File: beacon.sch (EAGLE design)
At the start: 49 parts, among them J1 5-5530843-0MALE, Q1 MMBT3904, Q2 DMG2302UK, U1 AOZ6662DI, U3 ATTINY85, U4 MS5637-02BA03, U5 SI4012, U6 MAAL-010704, U7 MIC5504

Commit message: Initial version of tracker schematic
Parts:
- R13: value 0R -> TBD
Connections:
- removed net DETECT: J1.5
- net OC1B: now also J1.5
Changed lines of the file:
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@@
 <part name="P+13" library="radio-tracker" deviceset="+3V3" device=""/>
 <part name="D1" library="radio-tracker" deviceset="LED" device=""/>
-<part name="R13" library="radio-tracker" deviceset="RESISTOR" device="0603" value="0R"/>
+<part name="R13" library="radio-tracker" deviceset="RESISTOR" device="0603" value="TBD"/>
 <part name="P+14" library="radio-tracker" deviceset="+3V3" device=""/>
 <part name="Z1" library="radio-tracker" deviceset="ABT-8" device="" package3d_urn="urn:adsk.eagle:package:18040019/1"/>
@@
 <label x="15.24" y="0" size="1.778" layer="95"/>
 </segment>
+<segment>
+<pinref part="J1" gate="G$1" pin="5"/>
+<wire x1="66.04" y1="5.08" x2="48.26" y2="5.08" width="0.1524" layer="91"/>
+<label x="48.26" y="5.08" size="1.778" layer="95"/>
+</segment>
 </net>
 <net name="VBAT" class="0">
@@
 </segment>
 </net>
-<net name="DETECT" class="0">
-<segment>
-<pinref part="J1" gate="G$1" pin="5"/>
-<wire x1="66.04" y1="5.08" x2="48.26" y2="5.08" width="0.1524" layer="91"/>
-<label x="48.26" y="5.08" size="1.778" layer="95"/>
-</segment>
-</net>

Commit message: Various schematic updates
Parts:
- LS1: value WT-1205 -> AT-1224-TWT-5V-2-R; device radio-tracker:WT-1205 -> radio-tracker:AT-1224-TWT-5V-2-R
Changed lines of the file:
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@@
 <part name="R12" library="radio-tracker" deviceset="RESISTOR" device="0603" value="1M"/>
 <part name="C14" library="radio-tracker" deviceset="CAPACITOR" device="0603" value="0.1uF"/>
-<part name="LS1" library="radio-tracker" deviceset="WT-1205" device="" package3d_urn="urn:adsk.eagle:package:18040044/1"/>
+<part name="LS1" library="radio-tracker" deviceset="AT-1224-TWT-5V-2-R" device="" package3d_urn="urn:adsk.eagle:package:18040044/1"/>
 <part name="GND20" library="radio-tracker" deviceset="GND" device=""/>
 <part name="P+12" library="radio-tracker" deviceset="+5V" device=""/>

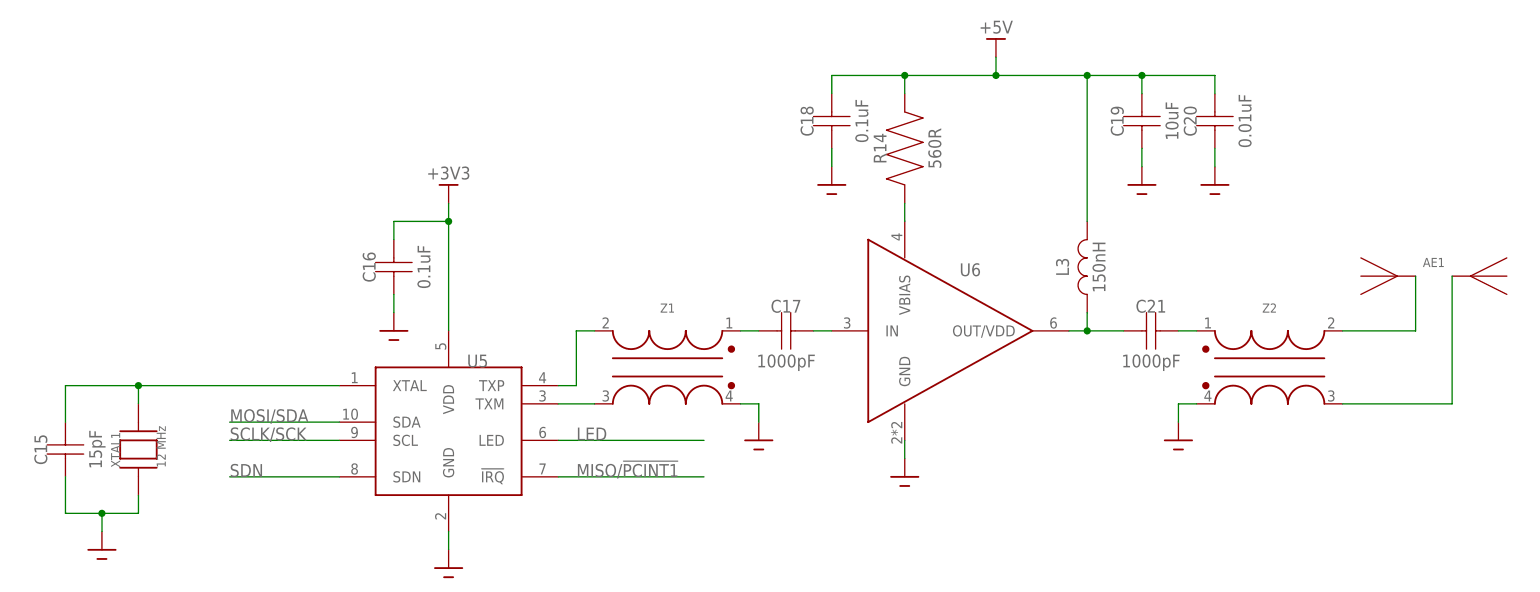
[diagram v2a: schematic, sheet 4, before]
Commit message: First routing attempt
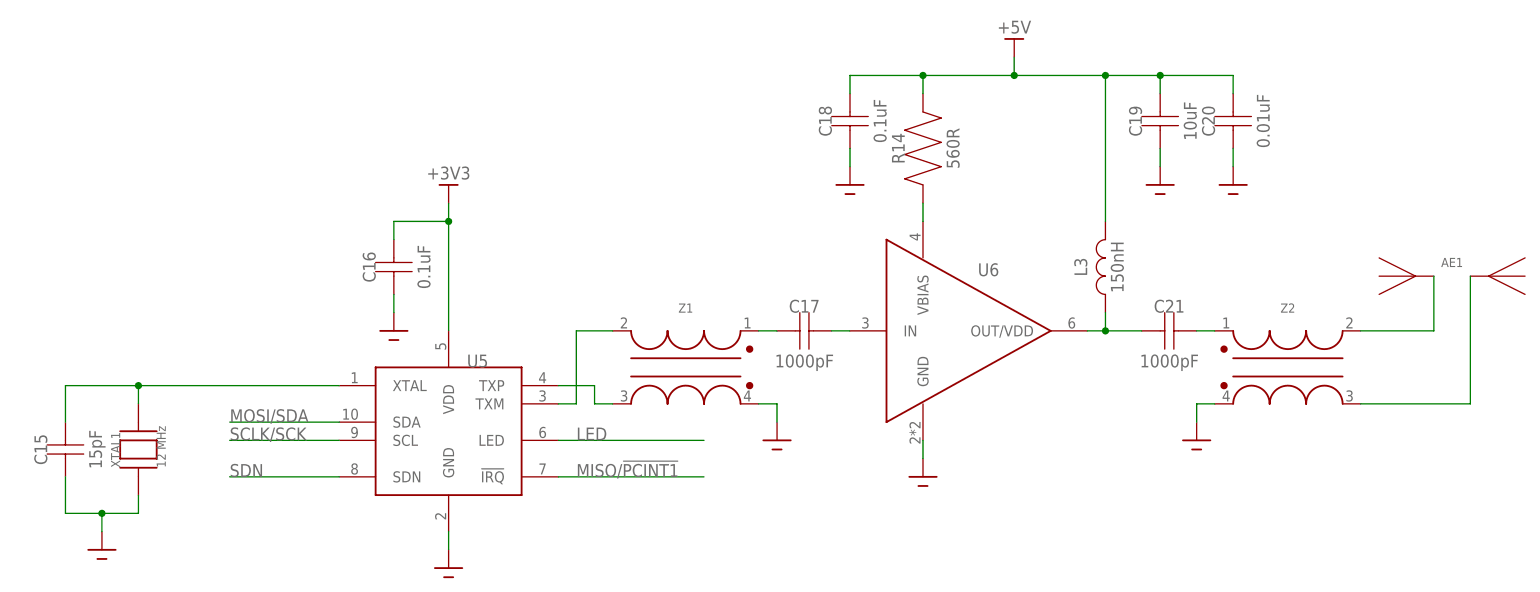
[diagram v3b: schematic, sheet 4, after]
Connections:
- removed net N$18: U5.TXM, Z1.BAL2
- removed net N$19: U5.TXP, Z1.BAL1
- new net N$10: U5.TXP, Z1.BAL2
- new net N$11: U5.TXM, Z1.BAL1
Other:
- moved on the sheet: AE1, C17, C18, C19, C20, C21, L3, R14, U6, Z1, Z2

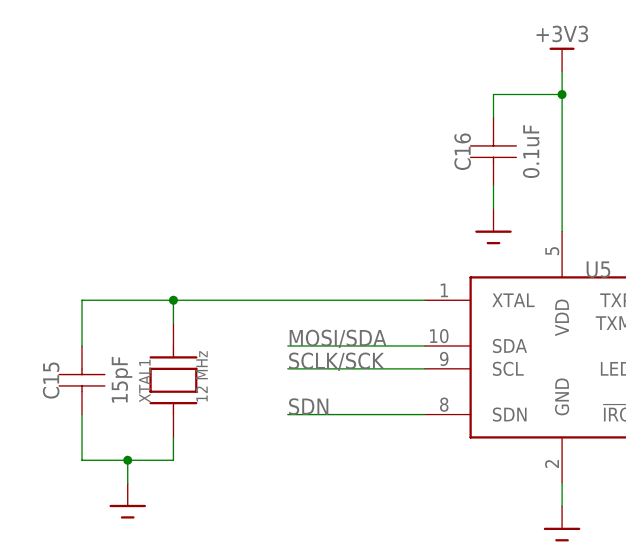
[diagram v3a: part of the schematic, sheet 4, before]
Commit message: Routed beacon
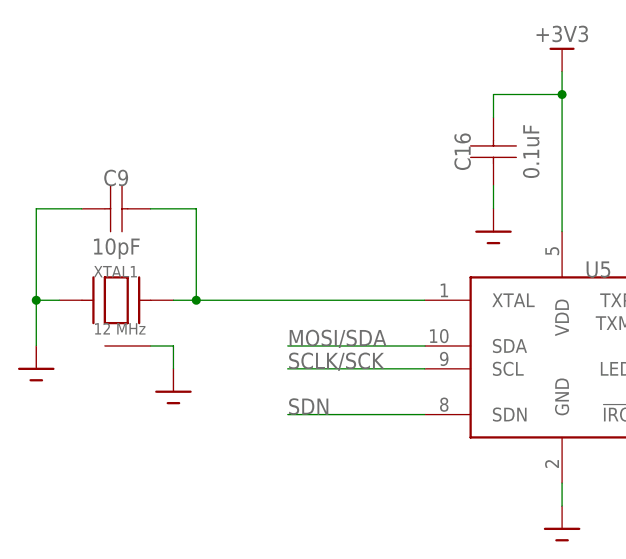
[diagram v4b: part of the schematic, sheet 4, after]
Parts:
- removed C15: 15pF, radio-tracker:CAPACITOR0603
- added C9: 10pF, radio-tracker:CAPACITOR0603
- XTAL1: device radio-tracker:ABLS -> radio-tracker:RH100
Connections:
- net !RESET: now also J1.9; no longer J1.6
- net +3V3: now also J1.4; no longer J1.1
- net +5V: now also J1.3; no longer J1.2
- net +9V: now also J1.2; no longer J1.3
- net GND: now also C9.P$1, XTAL1.GND; no longer C15.P$1
- net MISO/!PCINT1: now also J1.6; no longer J1.8
- net MOSI/SDA: now also J1.7; no longer J1.9
- net N$17: now also C9.P$2; no longer C15.P$2
- net OC1B: now also J1.8; no longer J1.5
- net SCLK/SCK: now also J1.5; no longer J1.7
- net VBAT: now also J1.1; no longer J1.4

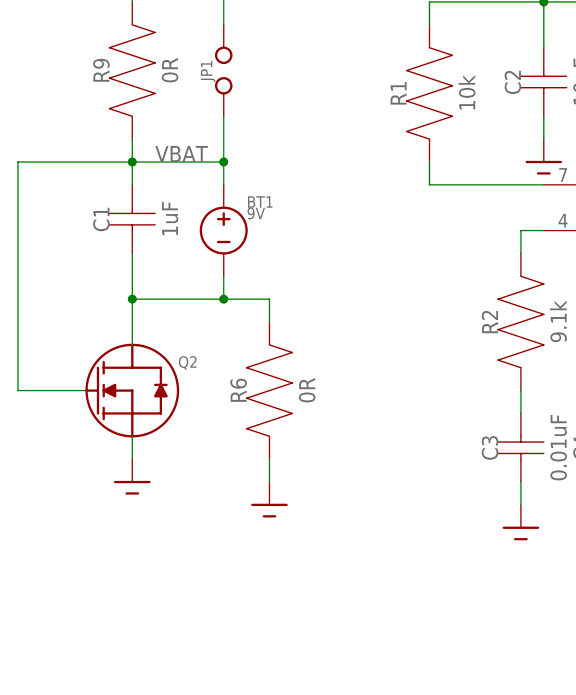
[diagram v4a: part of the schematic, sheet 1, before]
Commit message: Added PTC fuse
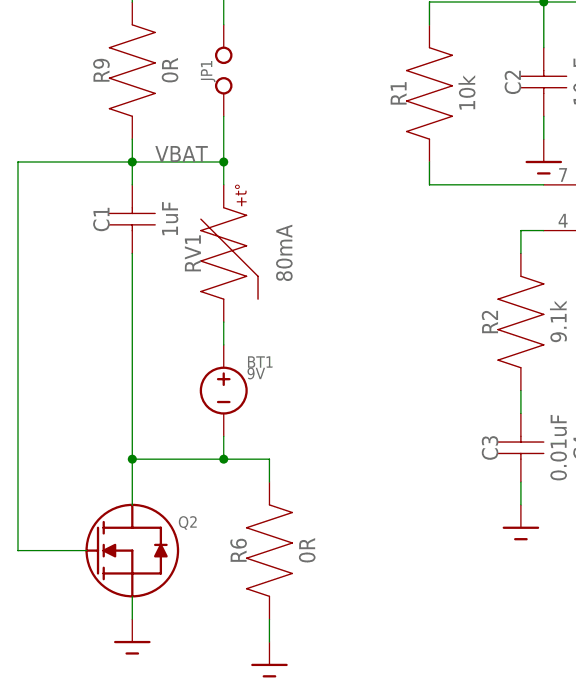
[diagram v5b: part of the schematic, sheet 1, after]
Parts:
- added RV1: 80mA, radio-tracker:PTC0603
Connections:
- new net N$12: BT1.P$2, RV1.P$1
- net VBAT: now also RV1.P$2; no longer BT1.P$2
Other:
- moved on the sheet: BT1, Q2, R6
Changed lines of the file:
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@@
 <part name="C9" library="radio-tracker" deviceset="CAPACITOR" device="0603" value="10pF"/>
 <part name="GND12" library="radio-tracker" deviceset="GND" device=""/>
+<part name="RV1" library="radio-tracker" deviceset="PTC" device="0603" value="80mA"/>
 </parts>
 <sheets>
@@
 </plain>
 <instances>
-<instance part="BT1" gate="G$1" x="2.54" y="-2.54" smashed="yes">
-<attribute name="NAME" x="5.08" y="0" size="1.27" layer="95"/>
-<attribute name="VALUE" x="5.08" y="0" size="1.27" layer="96" align="top-left"/>
-</instance>
-<instance part="GND1" gate="1" x="-7.62" y="-30.48" smashed="yes"/>
+<instance part="BT1" gate="G$1" x="2.54" y="-20.32" smashed="yes">
+<attribute name="NAME" x="5.08" y="-17.78" size="1.27" layer="95"/>
+<attribute name="VALUE" x="5.08" y="-17.78" size="1.27" layer="96" align="top-left"/>
+</instance>
+<instance part="GND1" gate="1" x="-7.62" y="-48.26" smashed="yes"/>
 <instance part="C1" gate="G$1" x="-7.62" y="-5.08" smashed="yes" rot="R90">
 <attribute name="NAME" x="-10.16" y="-1.27" size="1.778" layer="95" rot="R90" align="bottom-center"/>
@@
 <instance part="GND9" gate="1" x="154.94" y="-30.48" smashed="yes"/>
 <instance part="GND10" gate="1" x="175.26" y="-27.94" smashed="yes"/>
-<instance part="Q2" gate="G$1" x="-7.62" y="-20.32" smashed="yes">
-<attribute name="NAME" x="-2.54" y="-17.78" size="1.27" layer="95"/>
-</instance>
-<instance part="R6" gate="G$1" x="7.62" y="-27.94" smashed="yes" rot="R90">
-<attribute name="NAME" x="5.08" y="-20.32" size="1.778" layer="95" rot="R90" align="bottom-center"/>
-<attribute name="VALUE" x="12.7" y="-20.32" size="1.778" layer="96" rot="R90" align="bottom-center"/>
-</instance>
-<instance part="GND11" gate="1" x="7.62" y="-33.02" smashed="yes"/>
+<instance part="Q2" gate="G$1" x="-7.62" y="-38.1" smashed="yes">
+<attribute name="NAME" x="-2.54" y="-35.56" size="1.27" layer="95"/>
+</instance>
+<instance part="R6" gate="G$1" x="7.62" y="-45.72" smashed="yes" rot="R90">
+<attribute name="NAME" x="5.08" y="-38.1" size="1.778" layer="95" rot="R90" align="bottom-center"/>
+<attribute name="VALUE" x="12.7" y="-38.1" size="1.778" layer="96" rot="R90" align="bottom-center"/>
+</instance>
+<instance part="GND11" gate="1" x="7.62" y="-50.8" smashed="yes"/>
+<instance part="RV1" gate="G$1" x="2.54" y="-12.7" smashed="yes" rot="R90">
+<attribute name="NAME" x="0" y="-5.08" size="1.778" layer="95" rot="R90" align="bottom-center"/>
+<attribute name="VALUE" x="10.16" y="-5.08" size="1.778" layer="96" rot="R90" align="bottom-center"/>
+</instance>
 </instances>
 <busses>
@@
 <segment>
 <pinref part="Q2" gate="G$1" pin="S"/>
-<wire x1="-7.62" y1="-25.4" x2="-7.62" y2="-27.94" width="0.1524" layer="91"/>
+<wire x1="-7.62" y1="-43.18" x2="-7.62" y2="-45.72" width="0.1524" layer="91"/>
 <pinref part="GND1" gate="1" pin="GND"/>
 </segment>
@@
 <pinref part="R6" gate="G$1" pin="P$1"/>
 <pinref part="GND11" gate="1" pin="GND"/>
-<wire x1="7.62" y1="-27.94" x2="7.62" y2="-30.48" width="0.1524" layer="91"/>
+<wire x1="7.62" y1="-45.72" x2="7.62" y2="-48.26" width="0.1524" layer="91"/>
 </segment>
 </net>
@@
 <pinref part="C1" gate="G$1" pin="P$2"/>
 <wire x1="-7.62" y1="2.54" x2="-7.62" y2="5.08" width="0.1524" layer="91"/>
-<pinref part="BT1" gate="G$1" pin="P$2"/>
 <wire x1="-7.62" y1="5.08" x2="2.54" y2="5.08" width="0.1524" layer="91"/>
-<wire x1="2.54" y1="5.08" x2="2.54" y2="2.54" width="0.1524" layer="91"/>
 <pinref part="R9" gate="G$1" pin="P$1"/>
 <wire x1="-7.62" y1="7.62" x2="-7.62" y2="5.08" width="0.1524" layer="91"/>
@@
 <pinref part="JP1" gate="G$1" pin="P$1"/>
 <wire x1="2.54" y1="10.16" x2="2.54" y2="5.08" width="0.1524" layer="91"/>
-<junction x="2.54" y="5.08"/>
 <label x="-5.08" y="5.08" size="1.778" layer="95"/>
 <pinref part="Q2" gate="G$1" pin="G"/>
-<wire x1="-12.7" y1="-20.32" x2="-20.32" y2="-20.32" width="0.1524" layer="91"/>
-<wire x1="-20.32" y1="-20.32" x2="-20.32" y2="5.08" width="0.1524" layer="91"/>
+<wire x1="-12.7" y1="-38.1" x2="-20.32" y2="-38.1" width="0.1524" layer="91"/>
+<wire x1="-20.32" y1="-38.1" x2="-20.32" y2="5.08" width="0.1524" layer="91"/>
 <wire x1="-7.62" y1="5.08" x2="-20.32" y2="5.08" width="0.1524" layer="91"/>
+<pinref part="RV1" gate="G$1" pin="P$2"/>
+<wire x1="2.54" y1="2.54" x2="2.54" y2="5.08" width="0.1524" layer="91"/>
+<junction x="2.54" y="5.08"/>
 </segment>
 </net>
@@
 <segment>
 <pinref part="BT1" gate="G$1" pin="P$1"/>
-<wire x1="2.54" y1="-7.62" x2="2.54" y2="-10.16" width="0.1524" layer="91"/>
+<wire x1="2.54" y1="-25.4" x2="2.54" y2="-27.94" width="0.1524" layer="91"/>
 <pinref part="C1" gate="G$1" pin="P$1"/>
-<wire x1="2.54" y1="-10.16" x2="-7.62" y2="-10.16" width="0.1524" layer="91"/>
-<wire x1="-7.62" y1="-10.16" x2="-7.62" y2="-5.08" width="0.1524" layer="91"/>
+<wire x1="2.54" y1="-27.94" x2="-7.62" y2="-27.94" width="0.1524" layer="91"/>
+<wire x1="-7.62" y1="-27.94" x2="-7.62" y2="-5.08" width="0.1524" layer="91"/>
 <pinref part="Q2" gate="G$1" pin="D"/>
-<wire x1="-7.62" y1="-15.24" x2="-7.62" y2="-10.16" width="0.1524" layer="91"/>
-<junction x="-7.62" y="-10.16"/>
-<wire x1="2.54" y1="-10.16" x2="7.62" y2="-10.16" width="0.1524" layer="91"/>
-<junction x="2.54" y="-10.16"/>
+<wire x1="-7.62" y1="-33.02" x2="-7.62" y2="-27.94" width="0.1524" layer="91"/>
+<junction x="-7.62" y="-27.94"/>
+<wire x1="2.54" y1="-27.94" x2="7.62" y2="-27.94" width="0.1524" layer="91"/>
+<junction x="2.54" y="-27.94"/>
 <pinref part="R6" gate="G$1" pin="P$2"/>
-<wire x1="7.62" y1="-10.16" x2="7.62" y2="-12.7" width="0.1524" layer="91"/>
-</segment>
-</net>
+<wire x1="7.62" y1="-27.94" x2="7.62" y2="-30.48" width="0.1524" layer="91"/>
+</segment>
+</net>
+<net name="N$12" class="0">
+<segment>
+<pinref part="BT1" gate="G$1" pin="P$2"/>
+<pinref part="RV1" gate="G$1" pin="P$1"/>
+<wire x1="2.54" y1="-15.24" x2="2.54" y2="-12.7" width="0.1524" layer="91"/>
+</segment>
+</net>

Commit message: Layed out tracker board
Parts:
- added R7: 10k, radio-tracker:RESISTOR0603
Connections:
- net !RESET: now also R7.P$1
- net +3V3: now also R7.P$2
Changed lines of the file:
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@@
 <part name="GND12" library="radio-tracker" deviceset="GND" device=""/>
 <part name="RV1" library="radio-tracker" deviceset="PTC" device="0603" value="80mA"/>
+<part name="R7" library="radio-tracker" deviceset="RESISTOR" device="0603" value="10k"/>
+<part name="P+16" library="radio-tracker" deviceset="+3V3" device=""/>
 </parts>
 <sheets>
@@
 <attribute name="VALUE" x="30.48" y="-5.08" size="1.778" layer="96" rot="R180" align="bottom-center"/>
 </instance>
+<instance part="R7" gate="G$1" x="78.74" y="-30.48" smashed="yes" rot="R90">
+<attribute name="NAME" x="76.2" y="-22.86" size="1.778" layer="95" rot="R90" align="bottom-center"/>
+<attribute name="VALUE" x="83.82" y="-22.86" size="1.778" layer="96" rot="R90" align="bottom-center"/>
+</instance>
+<instance part="P+16" gate="G$1" x="78.74" y="-10.16" smashed="yes">
+<attribute name="VALUE" x="78.74" y="-7.62" size="1.778" layer="96" rot="R180" align="bottom-center"/>
+</instance>
 </instances>
 <busses>
@@
 <wire x1="43.18" y1="7.62" x2="66.04" y2="7.62" width="0.1524" layer="91"/>
 </segment>
+<segment>
+<pinref part="P+16" gate="G$1" pin="+3V3"/>
+<pinref part="R7" gate="G$1" pin="P$2"/>
+<wire x1="78.74" y1="-12.7" x2="78.74" y2="-15.24" width="0.1524" layer="91"/>
+</segment>
 </net>
 <net name="SDN" class="0">
@@
 <label x="48.26" y="-5.08" size="1.778" layer="95"/>
 </segment>
-</net>
+<segment>
+<pinref part="R7" gate="G$1" pin="P$1"/>
+<wire x1="78.74" y1="-30.48" x2="78.74" y2="-33.02" width="0.1524" layer="91"/>
+<wire x1="78.74" y1="-33.02" x2="66.04" y2="-33.02" width="0.1524" layer="91"/>
+<label x="66.04" y="-33.02" size="1.778" layer="95"/>
+</segment>
+</net>
